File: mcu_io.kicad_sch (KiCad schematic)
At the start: 11 parts, among them U3 SiWG917Y, U6 NC7SV17P5X

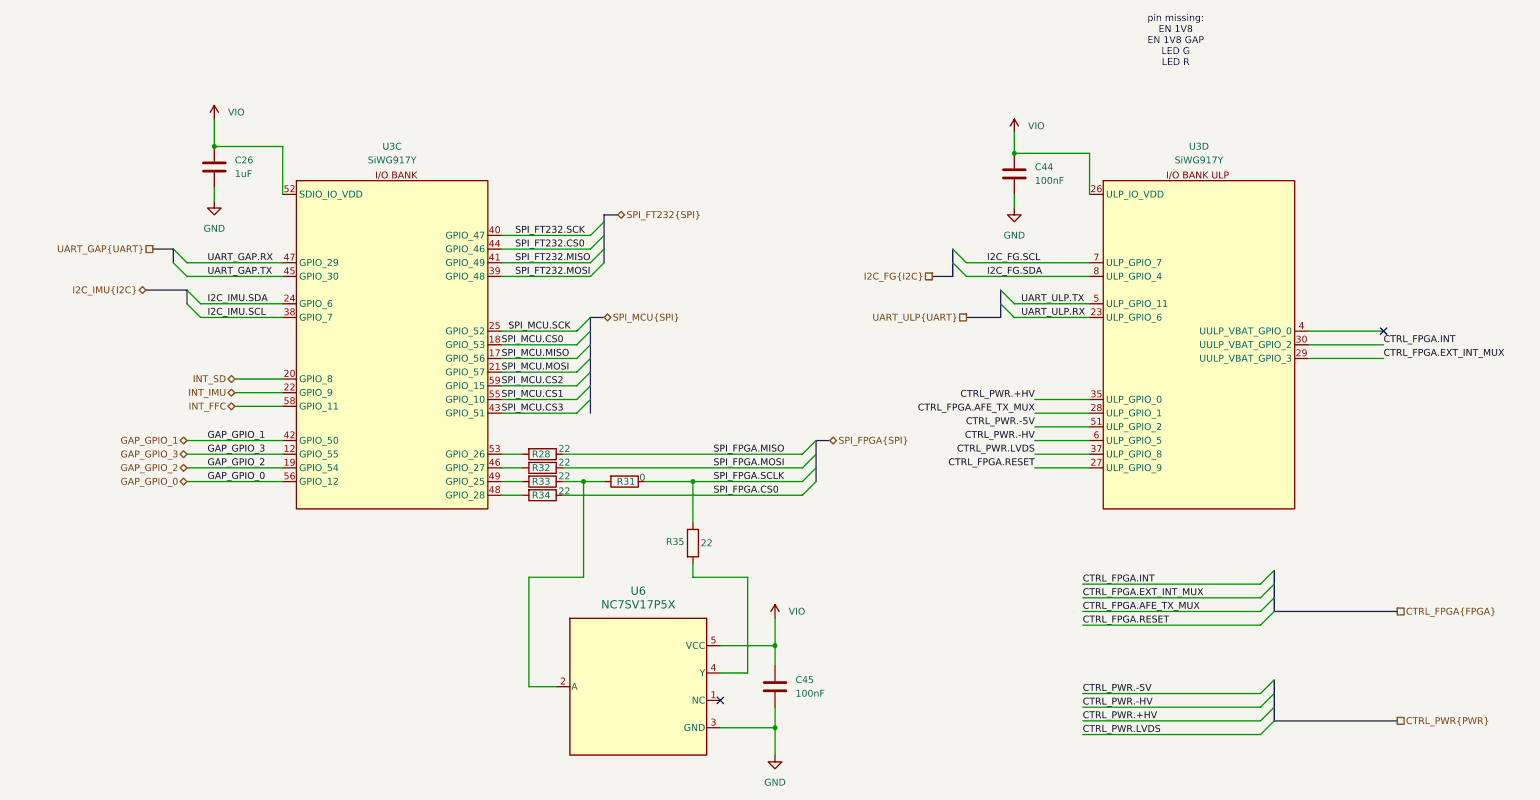
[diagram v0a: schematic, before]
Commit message: insert of gpio expander
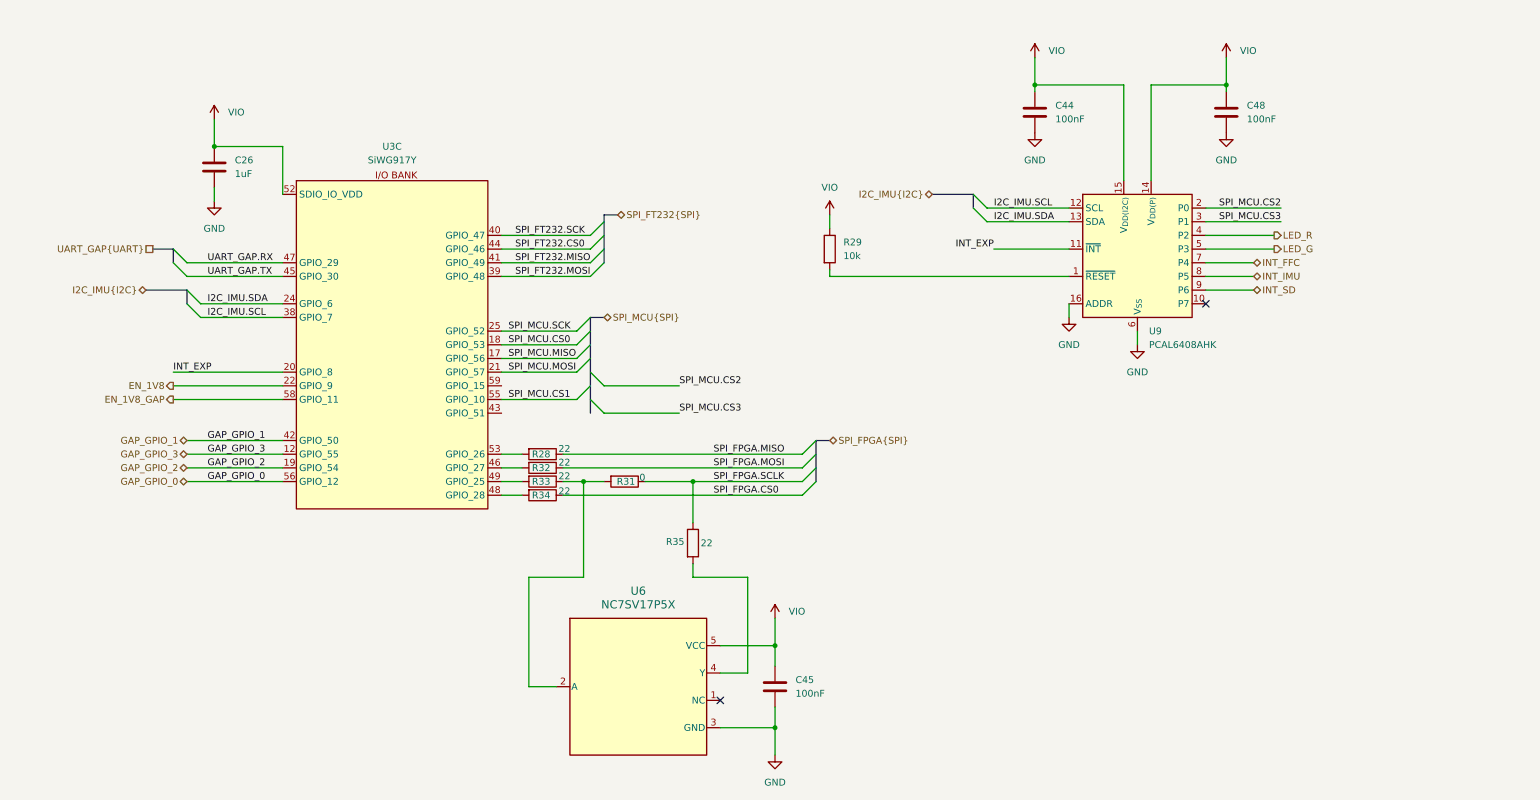
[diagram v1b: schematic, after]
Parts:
- removed unit 4 of U3
- added C48: 100nF, Capacitor_SMD:C_0402_1005Metric, symbol #dzdb:g_cap/C-100n-0402
- added R29: 10k, Resistor_SMD:R_0402_1005Metric, symbol #dzdb:g_res/R-10k-0402
- added U9: PCAL6408AHK, Package_DFN_QFN:UQFN-16_1.8x2.6mm_P0.4mm, symbol #dzdb:s_logic/L-NXP-PCAL6408AHK
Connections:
- net GND: now also C48.2, U9.16 (ADDR), U9.6 (V_{SS})
- net I2C_IMU.SCL: now also U9.12 (SCL)
- net I2C_IMU.SDA: now also U9.13 (SDA)
- net INT_FFC: now also U9.7 (P4); no longer U3.58 (GPIO_11)
- net INT_IMU: now also U9.8 (P5); no longer U3.22 (GPIO_9)
- net INT_SD: now also U9.9 (P6); no longer U3.20 (GPIO_8)
- net SPI_MCU.CS2: now also U9.2 (P0); no longer U3.59 (GPIO_15)
- net SPI_MCU.CS3: now also U9.3 (P1); no longer U3.43 (GPIO_51)
- net VIO: now also C48.1, R29.1, U9.14 (V_{DD(P)}), U9.15 (V_{DD(I2C)})
- new net: R29.2, U9.1 (~{RESET})
- new net EN_1V8: U3.22 (GPIO_9)
- new net EN_1V8_GAP: U3.58 (GPIO_11)
- new net INT_EXP: U3.20 (GPIO_8), U9.11 (~{INT})
- new net LED_G: U9.5 (P3)
- new net LED_R: U9.4 (P2)
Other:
- note removed: "pin missing: EN 1V8 EN 1V8 GAP LED G LED R"

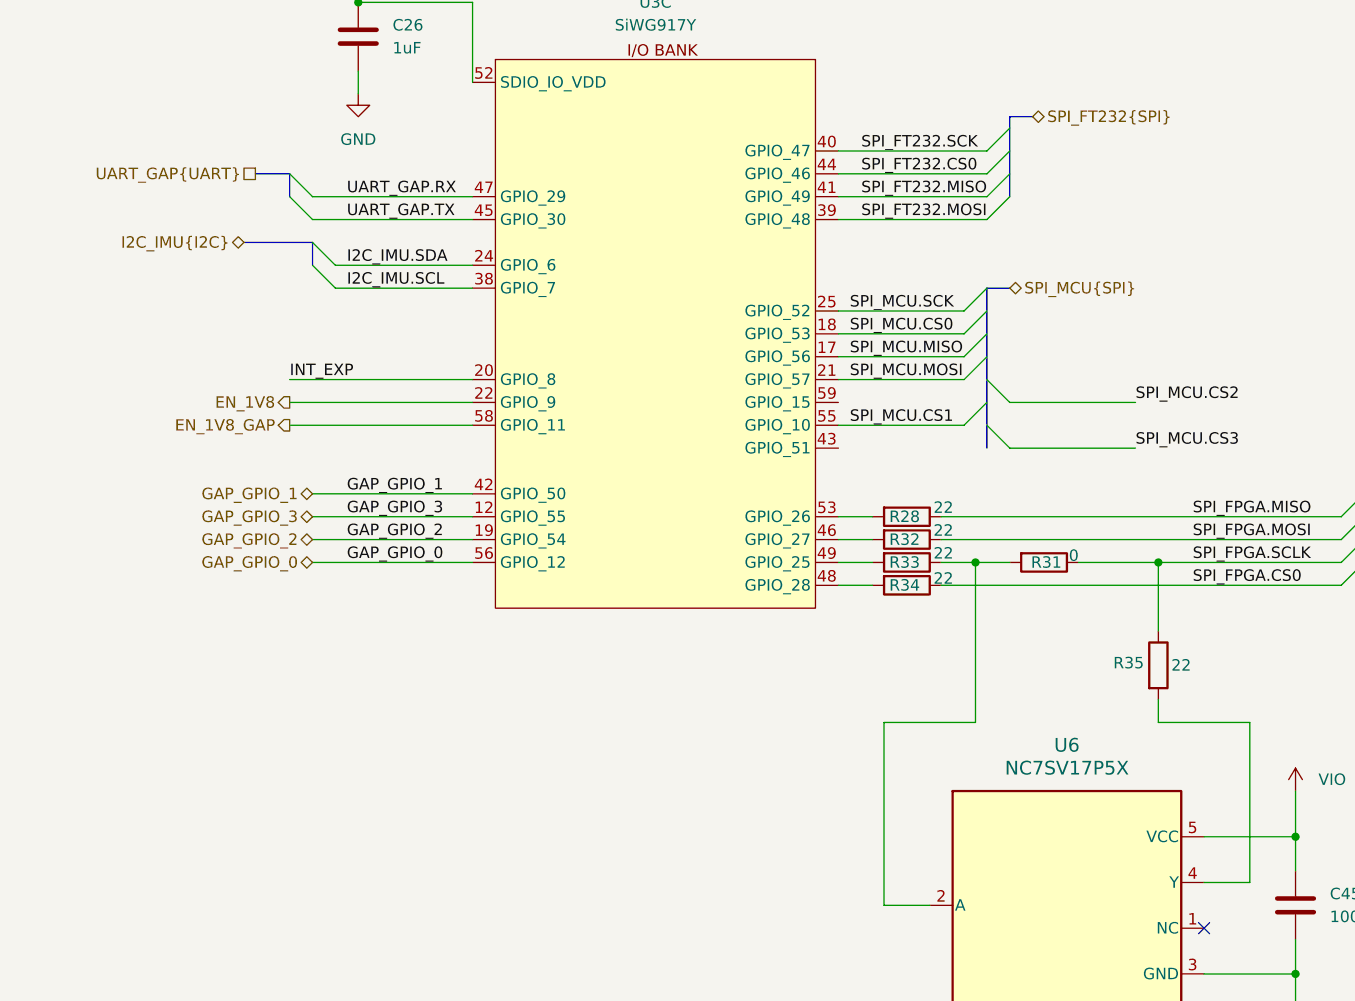
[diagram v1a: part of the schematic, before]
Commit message: added schematics comments of review 1
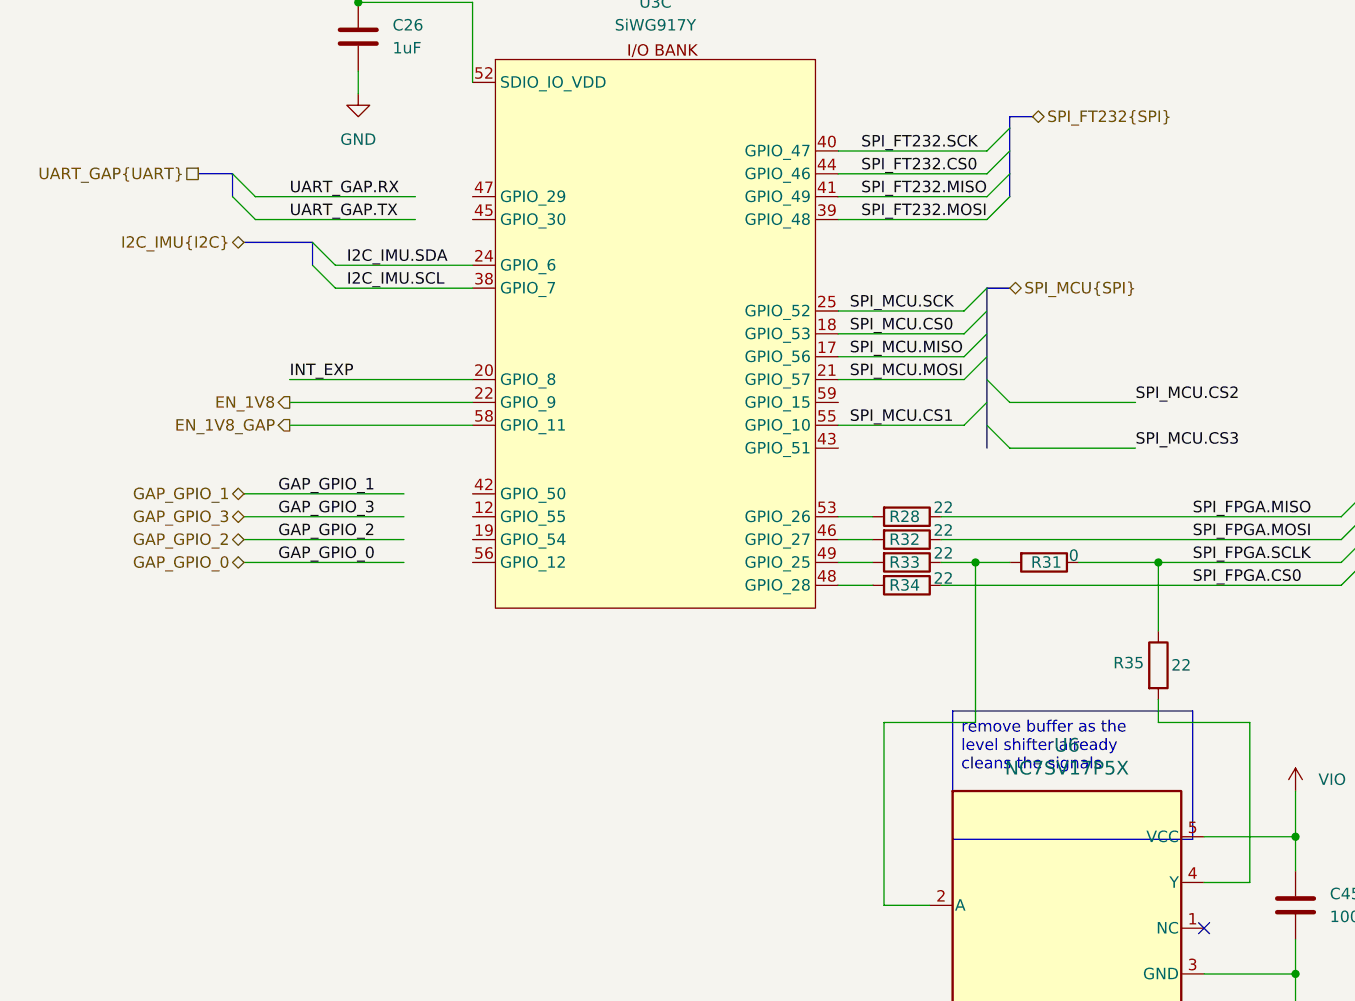
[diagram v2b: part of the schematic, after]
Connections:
- net GAP_GPIO_0: no longer U3.56 (GPIO_12)
- net GAP_GPIO_1: no longer U3.42 (GPIO_50)
- net GAP_GPIO_2: no longer U3.19 (GPIO_54)
- net GAP_GPIO_3: no longer U3.12 (GPIO_55)
- net UART_GAP.RX: no longer U3.47 (GPIO_29)
- net UART_GAP.TX: no longer U3.45 (GPIO_30)
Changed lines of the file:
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@@
 	(generator_version "10.0")
 	(paper "A4")
+	(text_box "remove buffer as the level shifter already cleans the signals"
+		(exclude_from_sim no)
+		(at 109.22 130.81 0)
+		(size 26.67 14.2494)
+		(margins 0.9525 0.9525 0.9525 0.9525)
+		(stroke
+			(width 0)
+			(type solid)
+		)
+		(fill
+			(type color)
+			(color 255 153 0 1)
+		)
+		(effects
+			(font
+				(size 1.27 1.27)
+			)
+			(justify left top)
+		)
+	)
 	(junction
 		(at 43.18 52.07)
@@
 	)
 	(bus_entry
-		(at 38.1 76.2)
+		(at 31.75 76.2)
 		(size -2.54 -2.54)
 		(stroke
@@
 	)
 	(bus_entry
-		(at 38.1 73.66)
+		(at 31.75 73.66)
 		(size -2.54 -2.54)
 		(stroke
@@
 	(wire
 		(pts
-			(xy 38.1 114.3) (xy 55.88 114.3)
+			(xy 30.48 114.3) (xy 48.26 114.3)
 		)
 		(stroke
@@
 	(bus
 		(pts
-			(xy 35.56 71.12) (xy 31.75 71.12)
+			(xy 29.21 71.12) (xy 25.4 71.12)
 		)
 		(stroke
@@
 	(wire
 		(pts
-			(xy 38.1 109.22) (xy 55.88 109.22)
+			(xy 30.48 109.22) (xy 48.26 109.22)
 		)
 		(stroke
@@
 	(wire
 		(pts
-			(xy 38.1 76.2) (xy 55.88 76.2)
+			(xy 31.75 76.2) (xy 49.53 76.2)
 		)
 		(stroke
@@
 	(bus
 		(pts
-			(xy 35.56 73.66) (xy 35.56 71.12)
+			(xy 29.21 73.66) (xy 29.21 71.12)
 		)
 		(stroke
@@
 	(wire
 		(pts
-			(xy 38.1 73.66) (xy 55.88 73.66)
+			(xy 31.75 73.66) (xy 49.53 73.66)
 		)
 		(stroke
@@
 	(wire
 		(pts
-			(xy 38.1 106.68) (xy 55.88 106.68)
+			(xy 30.48 106.68) (xy 48.26 106.68)
 		)
 		(stroke
@@
 	(wire
 		(pts
-			(xy 38.1 111.76) (xy 55.88 111.76)
+			(xy 30.48 111.76) (xy 48.26 111.76)
 		)
 		(stroke
@@
 	)
 	(label "GAP_GPIO_1"
-		(at 41.91 106.68 0)
+		(at 34.29 106.68 0)
 		(effects
 			(font
@@
 	)
 	(label "GAP_GPIO_0"
-		(at 41.91 114.3 0)
+		(at 34.29 114.3 0)
 		(effects
 			(font
@@
 	)
 	(label "UART_GAP.RX"
-		(at 41.91 73.66 0)
+		(at 35.56 73.66 0)
 		(effects
 			(font
@@
 	)
 	(label "GAP_GPIO_3"
-		(at 41.91 109.22 0)
+		(at 34.29 109.22 0)
 		(effects
 			(font
@@
 	)
 	(label "GAP_GPIO_2"
-		(at 41.91 111.76 0)
+		(at 34.29 111.76 0)
 		(effects
 			(font
@@
 	)
 	(label "UART_GAP.TX"
-		(at 41.91 76.2 0)
+		(at 35.56 76.2 0)
 		(effects
 			(font
@@
 	(hierarchical_label "GAP_GPIO_0"
 		(shape bidirectional)
-		(at 38.1 114.3 180)
+		(at 30.48 114.3 180)
 		(effects
 			(font
@@
 	(hierarchical_label "GAP_GPIO_3"
 		(shape bidirectional)
-		(at 38.1 109.22 180)
+		(at 30.48 109.22 180)
 		(effects
 			(font
@@
 	(hierarchical_label "GAP_GPIO_2"
 		(shape bidirectional)
-		(at 38.1 111.76 180)
+		(at 30.48 111.76 180)
 		(effects
 			(font
@@
 	(hierarchical_label "GAP_GPIO_1"
 		(shape bidirectional)
-		(at 38.1 106.68 180)
+		(at 30.48 106.68 180)
 		(effects
 			(font
@@
 	(hierarchical_label "UART_GAP{UART}"
 		(shape passive)
-		(at 31.75 71.12 180)
-		(effects
-			(font
+		(at 25.4 71.12 180)
+		(effects
+			(font

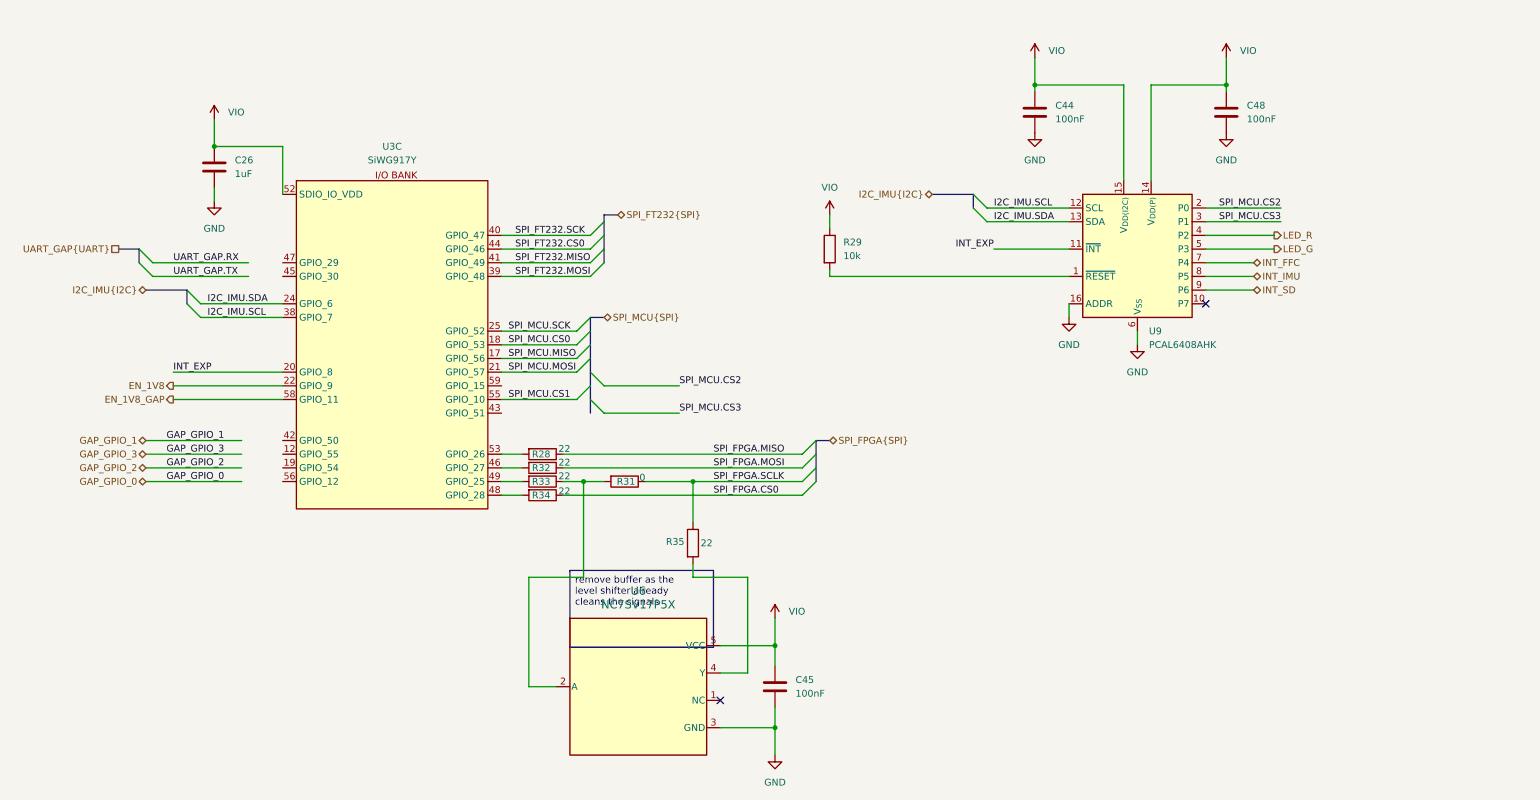
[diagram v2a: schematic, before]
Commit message: changes after first review: add lvl shifters, board at 1v8, new power tree
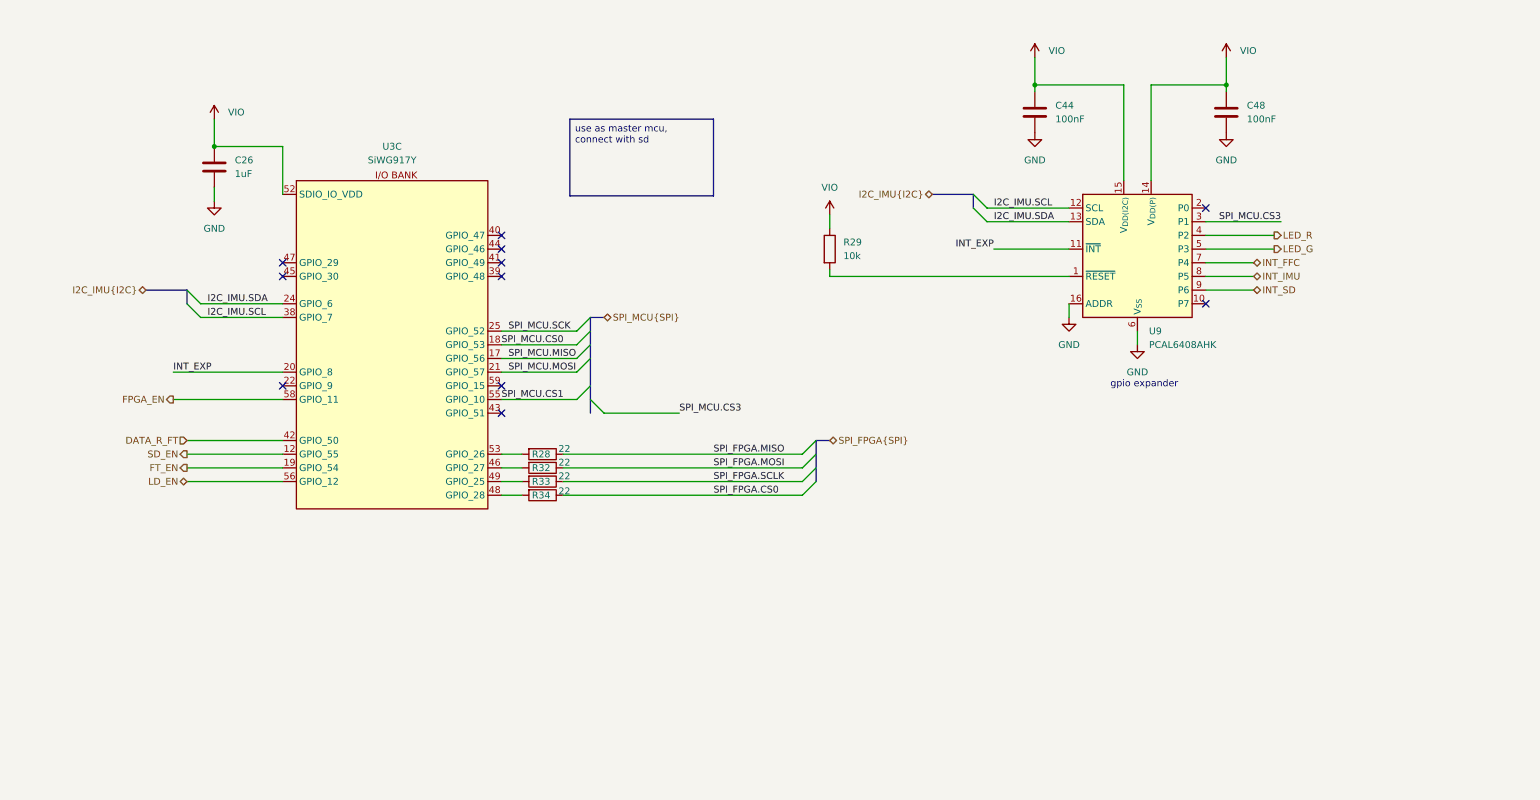
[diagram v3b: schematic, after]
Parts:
- removed C45: 100nF, Capacitor_SMD:C_0402_1005Metric, symbol #dzdb:g_cap/C-100n-0402
- removed R31: 0, Resistor_SMD:R_0402_1005Metric, symbol #dzdb:g_res/R-0-0402
- removed R35: 22, Resistor_SMD:R_0402_1005Metric, symbol #dzdb:g_res/R-22-0402
- removed U6: NC7SV17P5X, dz_ana:NC7SV17P5X, symbol #dzdb:s_logic/L-ONS-NC7SV17P5X
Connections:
- net SPI_FPGA.SCLK: now also R33.1
- net SD_EN: now reaches U3.12 (GPIO_55)
- net FT_EN: now reaches U3.19 (GPIO_54)
- net DATA_R_FT: now reaches U3.42 (GPIO_50)
- net LD_EN: now reaches U3.56 (GPIO_12)
- net EN_1V8: no longer names the net of U3.22 (GPIO_9)
- net EN_1V8_GAP renamed FPGA_EN
- net SPI_FT232.CS0: no longer names the net of U3.44 (GPIO_46)
- net SPI_FT232.MISO: no longer names the net of U3.41 (GPIO_49)
- net SPI_FT232.MOSI: no longer names the net of U3.39 (GPIO_48)
- net SPI_FT232.SCK: no longer names the net of U3.40 (GPIO_47)
- net SPI_MCU.CS2: no longer names the net of U9.2 (P0)
- no-connect marks 2 -> 11
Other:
- note added: "gpio expander"
